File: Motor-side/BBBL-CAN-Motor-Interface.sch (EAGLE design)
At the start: 2 parts

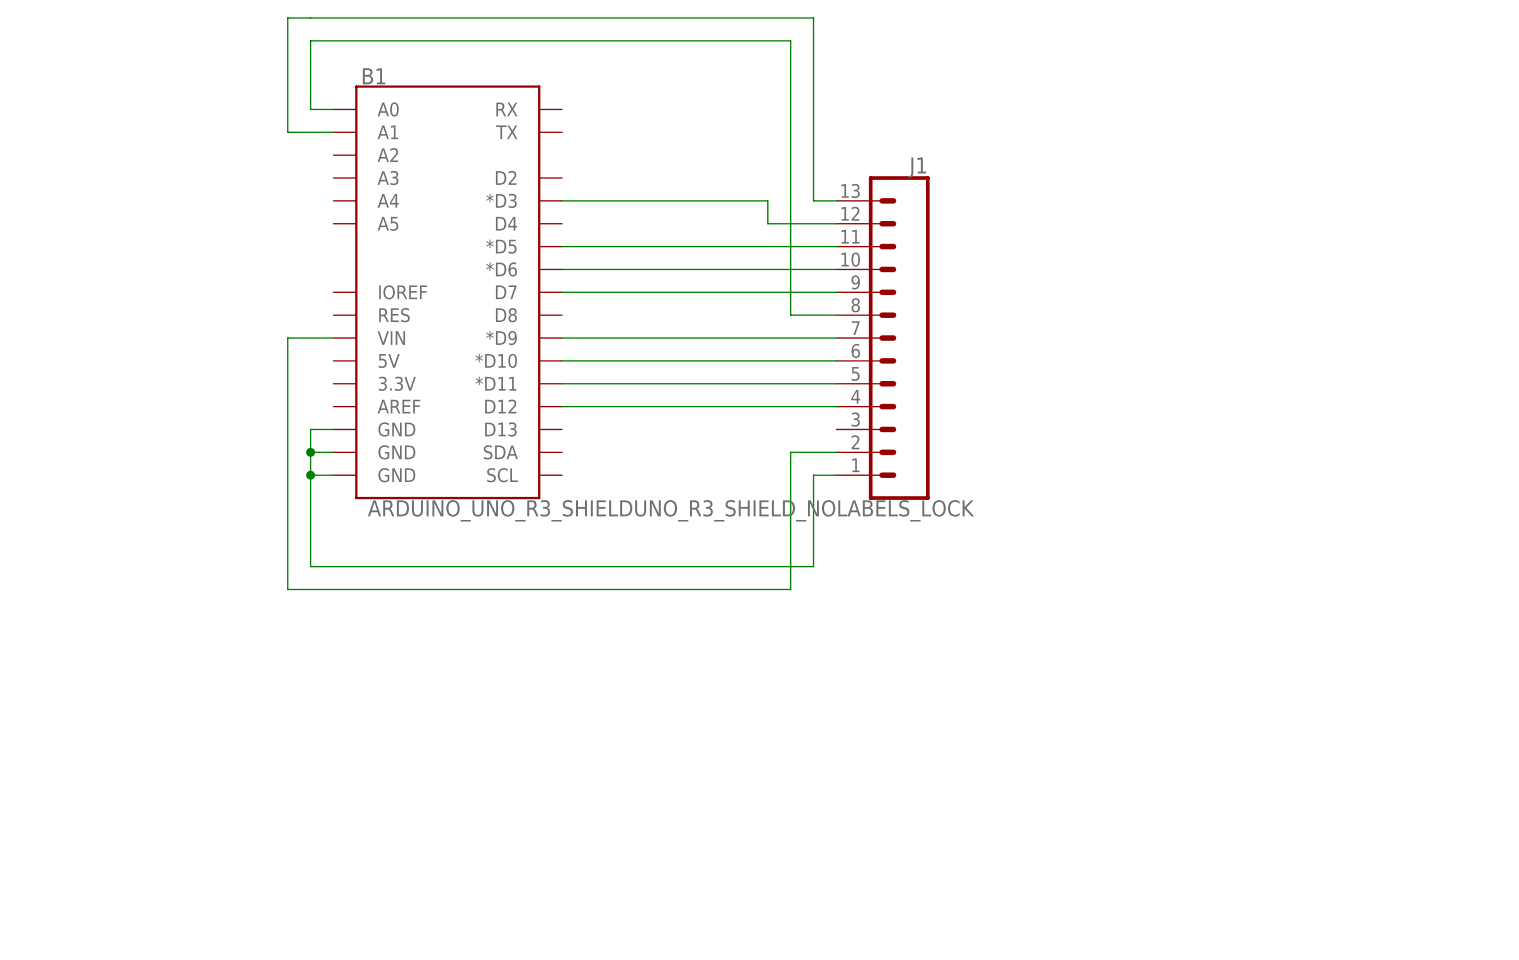
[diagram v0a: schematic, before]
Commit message: Modified Motor interface for non-interference with the CAN shield.
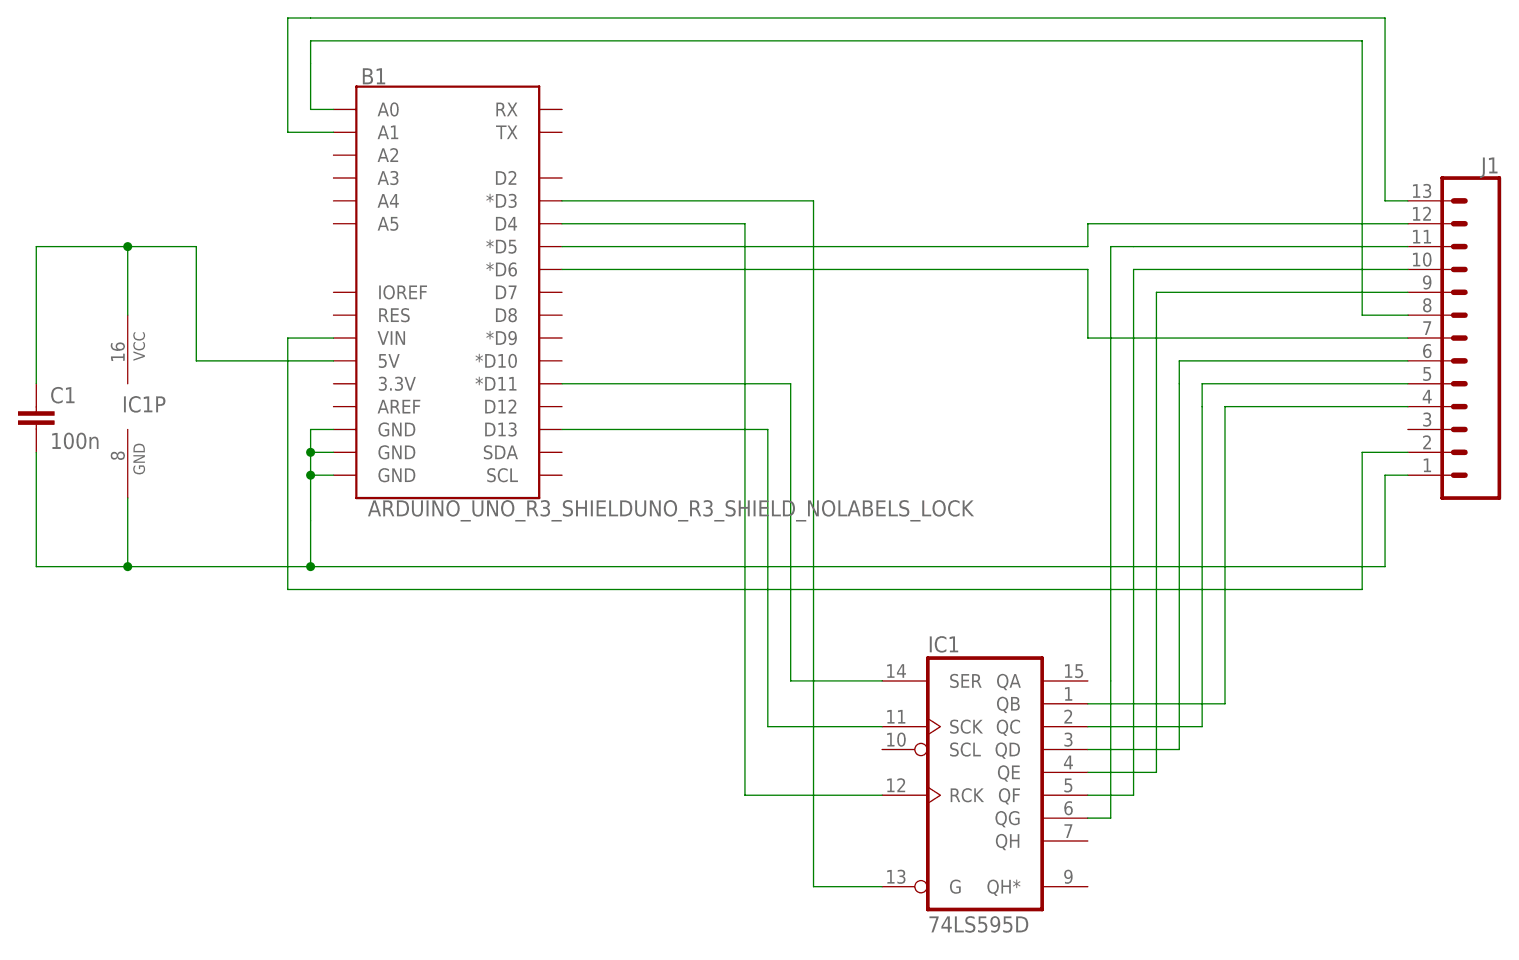
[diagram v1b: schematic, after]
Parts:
- added C1: 100n, resistor:C-EUC0603
- added IC1: 74LS595D, 74xx-us:74LS595D
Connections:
- new net N$1: B1.*D5, J1.12
- new net N$13: B1.*D11, IC1A.SER
- new net N$14: B1.D13, IC1A.SCK
- new net N$15: B1.D4, IC1A.RCK
- new net N$16: B1.5V, C1.1, IC1P.VCC
- net GND: now also C1.2, IC1P.GND
- net N$10: now also IC1A.QB, J1.4; no longer B1.*D11, J1.5
- net N$11: now also B1.*D3, IC1A.G; no longer B1.D12, J1.4
- net N$4: now also B1.*D6; no longer B1.*D9
- net N$5: now also IC1A.QG, J1.11; no longer B1.*D3, J1.12
- net N$6: now also IC1A.QF, J1.10; no longer B1.*D5, J1.11
- net N$7: now also IC1A.QE, J1.9; no longer B1.*D6, J1.10
- net N$8: now also IC1A.QD, J1.6; no longer B1.D7, J1.9
- net N$9: now also IC1A.QC, J1.5; no longer B1.*D10, J1.6
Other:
- moved on the sheet: J1
